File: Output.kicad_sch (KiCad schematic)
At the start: 44 parts, among them J21 GREEN_TS_OFF, J22 RED_IMD_FAULT, J23 RED_BMS_FAULT, J24 RGB_STRIP, J25 TSAL, J28 ADD_RGB_STRIP, Q10 SSM3K361TU,LF, Q11 SSM3K361TU,LF, Q3 2N7002NXAK, Q4 NTR5105PT1G, Q5 NTR5105PT1G, Q6 SSM3K361TU,LF, Q7 SSM3K361TU,LF, Q8 SSM3K361TU,LF, Q9 SSM3K361TU,LF

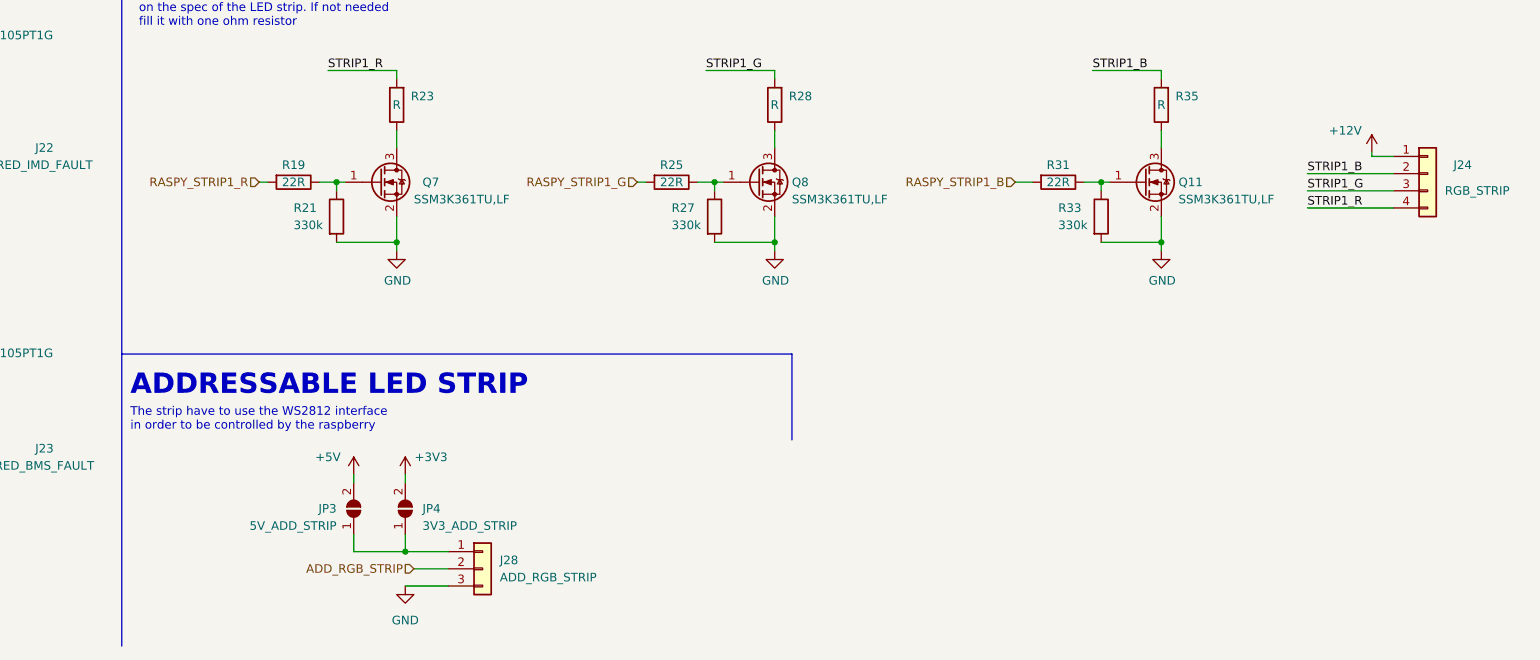
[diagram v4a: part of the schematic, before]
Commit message: Second iteration of the board layout. Need to fix some traces
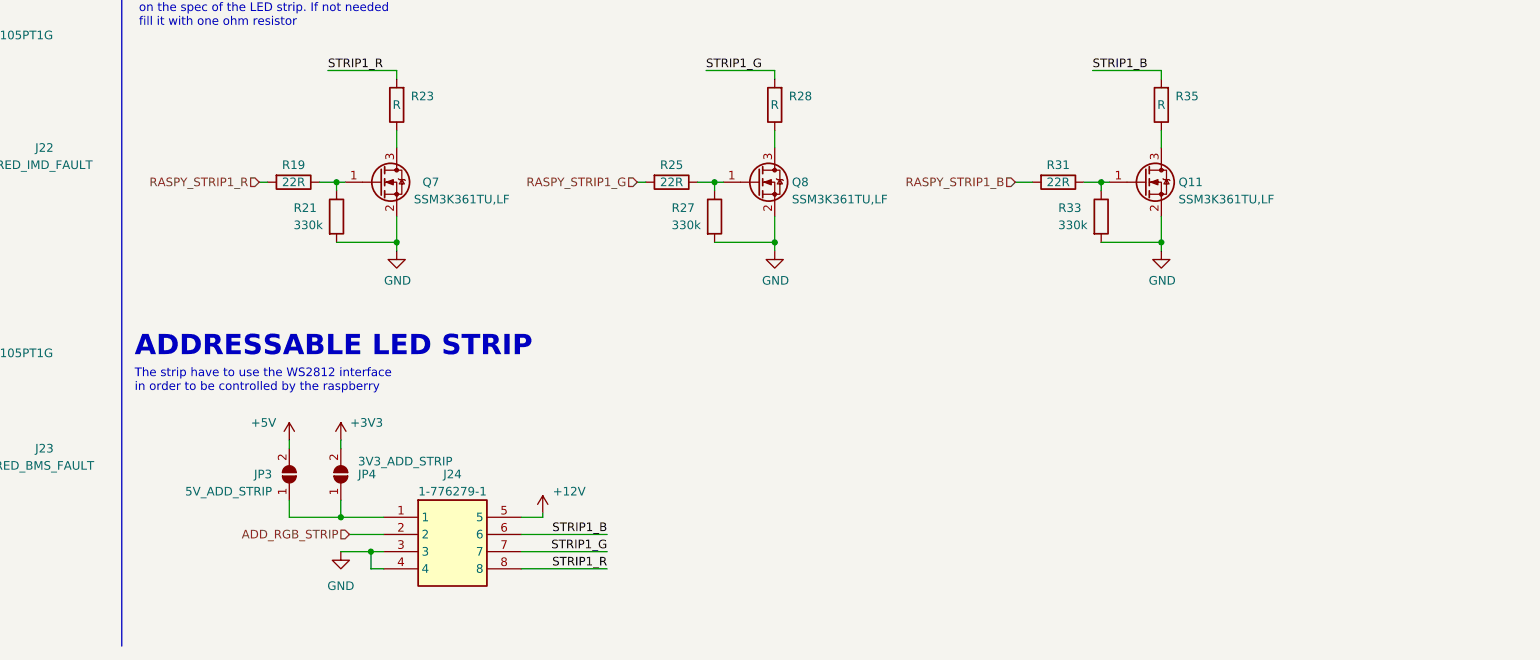
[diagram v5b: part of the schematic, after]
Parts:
- removed J24: RGB_STRIP, Connector_Molex:Molex_Micro-Fit_3.0_43650-0415_1x04_P3.00mm_Vertical, symbol Connector_Generic:Conn_01x04
- removed J28: ADD_RGB_STRIP, Connector_Molex:Molex_Micro-Fit_3.0_43650-0315_1x03_P3.00mm_Vertical, symbol Connector_Generic:Conn_01x03
- added J24: 1-776279-1, Eagle_Connectors:17762791, symbol 00_proj-lib:1-776279-1
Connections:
- net +12V: now also J24.5
- net ADD_RGB_STRIP: now also J24.2
- net GND: now also J24.3, J24.4
- net STRIP1_B: now also J24.6
- net STRIP1_G: now also J24.7
- net STRIP1_R: now also J24.8
- net at JP3.1 (A), JP4.1 (A): now also J24.1
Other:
- moved on the sheet: JP3, JP4
